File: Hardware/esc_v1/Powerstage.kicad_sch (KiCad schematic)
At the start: 0 parts

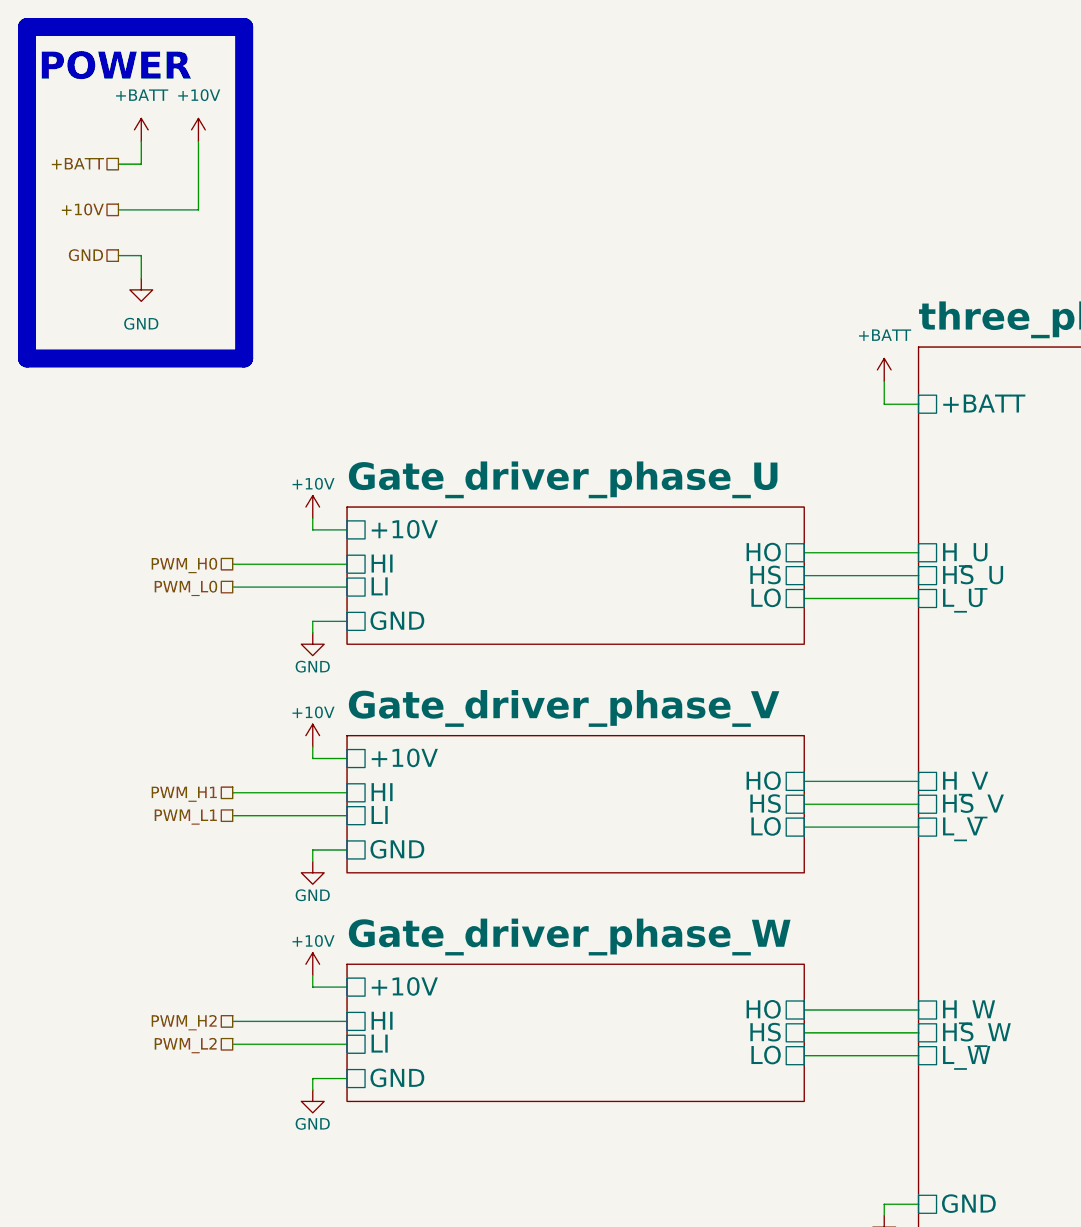
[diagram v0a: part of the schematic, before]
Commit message: changed gate driver, removed 10V buck and 5V LDO, added 5V buck. Started on Layout
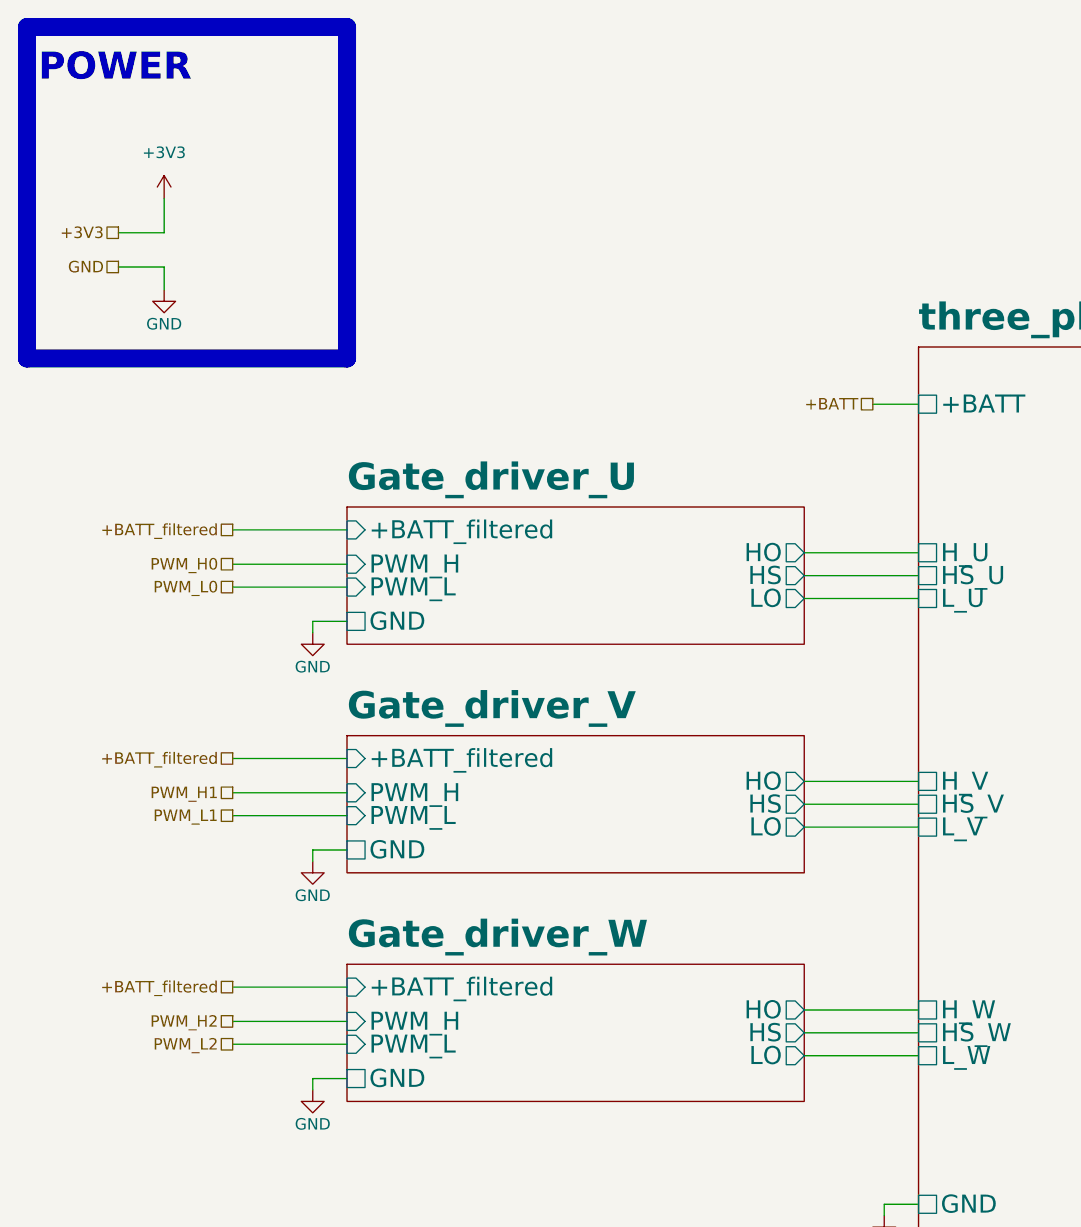
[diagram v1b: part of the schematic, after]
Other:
- removed sheet Gate_driver_phase_U
- removed sheet Gate_driver_phase_V
- removed sheet Gate_driver_phase_W
- added sheet Gate_driver_U (Gate_driver.kicad_sch)
- added sheet Gate_driver_V (Gate_driver.kicad_sch)
- added sheet Gate_driver_W (Gate_driver.kicad_sch)
